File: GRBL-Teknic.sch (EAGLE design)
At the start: 65 parts, among them IC3 LM1117, J1 POWER_JACKOVERPASTE_REDBOARD_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, J2 ICSP, Q1 ZXMP6A13FTA, Q2 2N7002PW, U1 FT231XS, U2 MIC5205, U3 ATMEGA328, Y1 16MHz

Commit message: working from adafruit metro now, simpest i could find
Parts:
- removed AD: (no value), SparkFun:M06SMD-STRAIGHT-COMBO
- removed C1, C14, C8: 0.1uF, SparkFun:CAP0603-CAP
- removed C13: 47pF, SparkFun-Capacitors:47PF-50V-5%(0603)
- removed C7: 1uF, SparkFun:CAP0603-CAP
- removed D1: MBRA140, SparkFun:DIODE-SCHOTTKY_
- removed F1: 500mA, SparkFun:PTCSMD
- removed FRAME2: FRAME-LETTER, SparkFun-Aesthetics:FRAME-LETTER
- removed IC3: LM1117, Testing:V_REG_LM1117ALT1
- removed IOL: (no value), SparkFun:M08SMD-COMBO
- removed J1: POWER_JACKOVERPASTE_REDBOARD_0603, Testing:POWER_JACKOVERPASTE_REDBOARD_0603
- removed J2: ICSP, SparkFun-Connectors:AVR_SPI_PRG_6SMT_MALE
- removed JP1: LOGO-SFENW2, SparkFun-Aesthetics:LOGO-SFENW2
- removed JP10: (no value), SparkFun-Connectors:M08SMD-COMBO
- removed JP2: M10SMD_COMBO, SparkFun-Connectors:M10SMD_COMBO
- removed JP3, JP4, JP5, JP6: STAND-OFF, SparkFun:STAND-OFF
- removed JP7: LOGO-SFESK, SparkFun-Aesthetics:LOGO-SFESK
- removed JP8, JP9: FIDUCIAL1X2, SparkFun:FIDUCIAL1X2
- removed LED1: Blue, SparkFun-LED:LED1206-NS
- removed LED2: Green, SparkFun-LED:LED1206-NS
- removed LED3: Red, SparkFun-LED:LED1206-NS
- removed LED4: Yellow, SparkFun-LED:LED1206-NS
- removed Q1: ZXMP6A13FTA, SparkFun:MOSFET-PCHANNELSMD
- removed Q2: 2N7002PW, SparkFun-DiscreteSemi:MOSFET-NCHANNEL2N7002PW
- removed R1, R6, R7, R9: 1k, SparkFun:RESISTOR0603-RES
- removed R10: 27, SparkFun-Resistors:RESISTOR0603-RES
- removed R12, R3: 10k, SparkFun:RESISTOR0603-RES
- removed R14: 715, SparkFun:RESISTOR0603-RES
- removed R15: 240, SparkFun:RESISTOR0603-RES
- removed S1: RESET, SparkFun:TAC_SWITCHSMD
- removed TP1, TP2, TP3, TP4, TP5, TP6: TP-3x5, SparkFun-Passives:TEST-POINT3X5
- removed U$13: USB-MINIB-5PIN, SparkFun-Connectors:USB-MINIB-5PIN
- removed U$16: OSHW-LOGOS, SparkFun-Aesthetics:OSHW-LOGOS
- removed U3: ATMEGA328, SparkFun:ATMEGA168
- removed Y1: 16MHz, SparkFun-FreqCtrl:RESONATORSMD
- added ATX-POWER: 35318-0620, con-molex-2:555X-6H
- added D3: MBR120, microbuilder:DIODE-SCHOTTKYSOD-123
- added L: RED, microbuilder:LED0805_NOOUTLINE
- added ON: GREEN, microbuilder:LED0805_NOOUTLINE
- added POWER1: 20610, microbuilder:HEADER-1X870MIL
- added RESET: KMR2, microbuilder:SWITCH_TACT_SMT4.6X2.8
- added RXLED, TXLED: YELLOW, microbuilder:LED0805_NOOUTLINE
- added U4: FT231XQ-x, microbuilder:FT231X
- added VSELECT: (no value), microbuilder:SOLDERJUMPER_2WAY
- added X-MOTOR, Y-MOTOR-1, Y-MOTOR-2, Y-MOTOR-3: 35318-0820, con-molex-2:555X-8H
- added X3: 20329, microbuilder:USB_W_SHIELD_20329
- added Y2: CSTCE16M0V53-R0 16MHZ, SmartPrj:RESONATORMU
- C10, C4: device SparkFun:CAP0603-CAP -> microbuilder:CAP_CERAMIC0805-NOOUTLINE
- C12, C2: value 0.1uF -> 10uF; device SparkFun:CAP0603-CAP -> microbuilder:CAP_CERAMIC0805-NOOUTLINE
- C15: value 10uF -> 0.1uF; device SparkFun-Capacitors:CAP_POL1206 -> microbuilder:CAP_CERAMIC0805-NOOUTLINE
- C3: device SparkFun:CAP_POL1206 -> microbuilder:CAP_CERAMIC0805-NOOUTLINE
- C5: value 47uF -> 0.1uF; device SparkFun:CAP_POLD -> microbuilder:CAP_CERAMIC_0805MP
- C6: value 10uF -> 0.1uF; device SparkFun:CAP_POL1206 -> microbuilder:CAP_CERAMIC0805-NOOUTLINE
- C9: value 47pF -> 0.1uF; device SparkFun-Capacitors:47PF-50V-5%(0603) -> microbuilder:CAP_CERAMIC0805-NOOUTLINE
- R11: value 10k -> 1K; device SparkFun:RESISTOR0603-RES -> microbuilder:RESISTOR0805_NOOUTLINE
- R2: value 1k -> 1K; device SparkFun:RESISTOR0603-RES -> microbuilder:RESISTOR_4PACK
- R4: value 10k -> 22; device SparkFun:RESISTOR0603-RES -> microbuilder:RESISTOR0805_NOOUTLINE
- R5: value 27 -> 22; device SparkFun-Resistors:RESISTOR0603-RES -> microbuilder:RESISTOR_0805MP
- R8: value 1k -> 10K; device SparkFun:RESISTOR0603-RES -> microbuilder:RESISTOR0805_NOOUTLINE
- U1: value FT231XS -> MIC5225-5.0; device SparkFun-DigitalIC:FT231XS -> microbuilder:VREG_SOT23-5
- U2: value MIC5205 -> ATmega328P-MU; device SparkFun:V_REG_LDOSMD -> microbuilder:ATMEGA328P
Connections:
- removed net 5V: C2.2, C3.+, C4.1, IC3.OUT, IC3.OUT@1, J2.2, JP10.4, JP10.7, Q1.S, R12.2, R15.2, R2.2, R3.2, R4.2, R6.1, R7.1, TP1.1, U2.EN, U2.IN, U3.AVCC, U3.VCC@1, U3.VCC@2
- removed net INSERT: J1.GND, Q1.G, R4.1
- removed net N$12: Q2.S, R11.1, U1.!DTR
- removed net N$15: IC3.ADJ, R14.2, R15.1
- removed net N$2: LED2.A, R2.1
- removed net N$8: LED3.A, R6.2
- removed net PWRIN: D1.A, J1.PWR
- removed net RX-I: IOL.1, R8.1, U3.PD0(RXD)
- removed net RXLED: LED4.C, U1.CBUS1
- removed net TX-O: IOL.2, R9.1, U3.PD1(TXD)
- removed net TXLED: LED3.C, U1.CBUS2
- removed net USBVCC: C12.1, C15.+, F1.2, Q1.D, U1.VCC
- removed net VUSB: C10.1, F1.1, U$13.VBUS
- new net +5V: C15.1, C2.2, D3.C, ON.A, POWER1.4, RXLED.A, TXLED.A, U1.OUT, U4.VCC, VSELECT.3
- new net IO0: R11.1, U2.(RXD)PD0
- new net N$5: R2G$2.2, RXLED.C
- new net N$9: R4.2, U4.USB_DM
- new net VBUS: D3.A, POWER1.1, X3CONN.VBUS
- new net VCCIO: C10.2, C6.2, R8.2, U2.AVCC, U2.VCC, VSELECT.2
- new net XTAL1: U2.XTAL1, Y2.3
- new net XTAL2: U2.XTAL2, Y2.1
- net 3.3V: now also C3.2, C9.1, POWER1.3, U4.3V3OUT(50MA), U4.RESET#, U4.VCCIO, VSELECT.1; no longer C14.1, C6.+, C7.1, JP10.5, Q2.G, R11.2, U1.!RESET, U1.3V3OUT, U1.VCCIO, U2.OUT
- net AD0: now also U2.(ADC0)PC0; no longer AD.1, U3.PC0(ADC0)
- net AD1: now also U2.(ADC1)PC1; no longer AD.2, U3.PC1(ADC1)
- net AD2: now also U2.(ADC2)PC2; no longer AD.3, U3.PC2(ADC2)
- net AD3: now also U2.(ADC3)PC3; no longer AD.4, U3.PC3(ADC3)
- net AD4/SDA: now also U2.(ADC4)PC4; no longer AD.5, JP2.2, U3.PC4(ADC4/SDA)
- net AD5/SCL: now also U2.(ADC5)PC5; no longer AD.6, JP2.1, U3.PC5(ADC5/SCL)
- net AREF: now also C4.2, POWER1.8, U2.AREF; no longer C1.1, JP2.3, U3.AREF
- net D+: now also R5.1, X3CONN.D+; no longer C9.1, R10.1, U$13.D+
- net D-: now also R4.1, X3CONN.D-; no longer C13.1, R5.1, U$13.D-
- net DTR: now also C5.1, U4.DTR#; no longer C8.1, Q2.D, R12.1
- net GND: now also ATX-POWER-4.S, C10.1, C15.2, C3.1, C4.1, C6.1, POWER1.5, POWER1.6, R2G$3.1, R2G$4.1, RESET.P, RESET.P1, U1.GND, U2.AGND, U4.CBUS3/SLEEP, U4.GND, X-MOTOR-5.S, X-MOTOR-6.S, X-MOTOR-7.S, X-MOTOR-8.S, X3CONN.GND, X3SHIELD.1, Y-MOTOR-1-5.S, Y-MOTOR-1-6.S, Y-MOTOR-1-7.S, Y-MOTOR-1-8.S, Y-MOTOR-2-5.S, Y-MOTOR-2-6.S, Y-MOTOR-2-7.S, Y-MOTOR-2-8.S, Y-MOTOR-3-5.S, Y-MOTOR-3-6.S, Y-MOTOR-3-7.S, Y-MOTOR-3-8.S, Y2.2; no longer C1.2, C10.2, C13.2, C14.2, C15.-, C3.-, C4.2, C5.-, C6.-, C7.2, J1.GNDBREAK, J2.6, JP10.2, JP10.3, JP2.4, LED1.C, LED2.C, R14.1, S1.1, S1.2, TP3.1, U$13.GND, U$13.MTN1, U$13.MTN2, U$13.MTN3, U$13.MTN4, U1.GND@16, U1.GND@6, U3.AGND, U3.GND@1, U3.GND@2, Y1.2
- net IO2: now also U2.(INT0)PD2, X-MOTOR-2.S; no longer IOL.3, U3.PD2(INT0)
- net IO3: now also U2.(INT1)PD3, Y-MOTOR-1-2.S, Y-MOTOR-2-2.S; no longer IOL.4, U3.PD3(INT1)
- net IO4: now also U2.(TO)PD4, Y-MOTOR-3-2.S; no longer IOL.5, U3.PD4(XCK/T0)
- net IO5: now also U2.(T1)PD5, X-MOTOR-3.S; no longer IOL.6, U3.PD5(T1)
- net IO6: now also U2.(AIN0)PD6, Y-MOTOR-1-3.S, Y-MOTOR-2-3.S; no longer IOL.7, U3.PD6(AIN0)
- net IO7: now also U2.(AIN1)PD7, Y-MOTOR-3-3.S; no longer IOL.8, U3.PD7(AIN1)
- net IO8: now also U2.(ICP)PB0, X-MOTOR-4.S, Y-MOTOR-1-4.S, Y-MOTOR-2-4.S, Y-MOTOR-3-4.S; no longer JP2.10, U3.PB0(ICP)
- net IO9: now also U2.(OC1)PB1; no longer JP2.9, U3.PB1(OC1A)
- net MISO: now also U2.(MISO)PB4; no longer J2.1, JP2.6, TP4.1, U3.PB4(MISO)
- net MOSI: now also U2.(MOSI)PB3; no longer J2.4, JP2.7, TP2.1, U3.PB3(MOSI/OC2)
- net N$1: now also L.C, R2G$4.2; no longer LED1.A, R1.2
- net N$10: now also R5.2, U4.UDB_DP; no longer LED4.A, R7.2
- net N$3: now also ON.C, R2G$3.2; no longer U3.PB6(XTAL1/TOSC1), Y1.1
- net N$4: now also R2G$2.1, U4.CBUS1/RXLED; no longer U3.PB7(XTAL2/TOSC2), Y1.3
- net N$6: now also R2G$1.1, U4.CBUS2/TXLED; no longer R5.2, U1.USBDM
- net N$7: now also R2G$1.2, TXLED.C; no longer R10.2, U1.USBDP
- net RESET: now also C5.2, POWER1.2, R8.1, RESET.S, RESET.S1, U2.RESET; no longer C8.2, J2.5, JP10.6, R3.1, S1.3, S1.4, TP6.1, U3.PC6(/RESET)
- net RXD: now also R11.2, U4.TXD-OUT; no longer R9.2, U1.RXD
- net SCK: now also L.A, U2.(SCK)PB5; no longer J2.3, JP2.5, R1.1, TP5.1, U3.PB5(SCK)
- net SS: now also U2.(SS)PB2; no longer JP2.8, U3.PB2(SS/OC1B)
- net TXD: now also U2.(TXD)PD1, U4.RXD-IN; no longer R8.2, U1.TXD
- net VIN: now also ATX-POWER-1.S, C12.1, POWER1.7, U1.EN, U1.IN; no longer C5.+, D1.C, IC3.IN, JP10.1
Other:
- note added: "ATMEGA328 MCU"
- note added: "DTR triggers reset"
- note added: "Default = 5V Cut trace and solder to 3V3 to change"
- note added: "IO LEVEL SELECTION"
- note added: "POWER LED"
- note added: "POWER SUPPLY: 3.3V"
- note added: "POWER SUPPLY: 5V"
- note added: "SCK LED"
- note added: "Teknic Motor Connectors"
- note added: "USB/Serial Bridge"
- note removed: "3.3V 150mA Out"
- note removed: "ATmega328"
- note removed: "Based on Arduino by: M.Banzi, D.Cuartielles, T.Igoe, G.Martino, D.Mellis"
- note removed: "FT231XS (USB-to-Serial Converter)"
- note removed: "Jim Lindblom"
- note removed: "Power Supply"
- note removed: "v21"
- moved on the sheet: C10, C12, C2, C4, C9

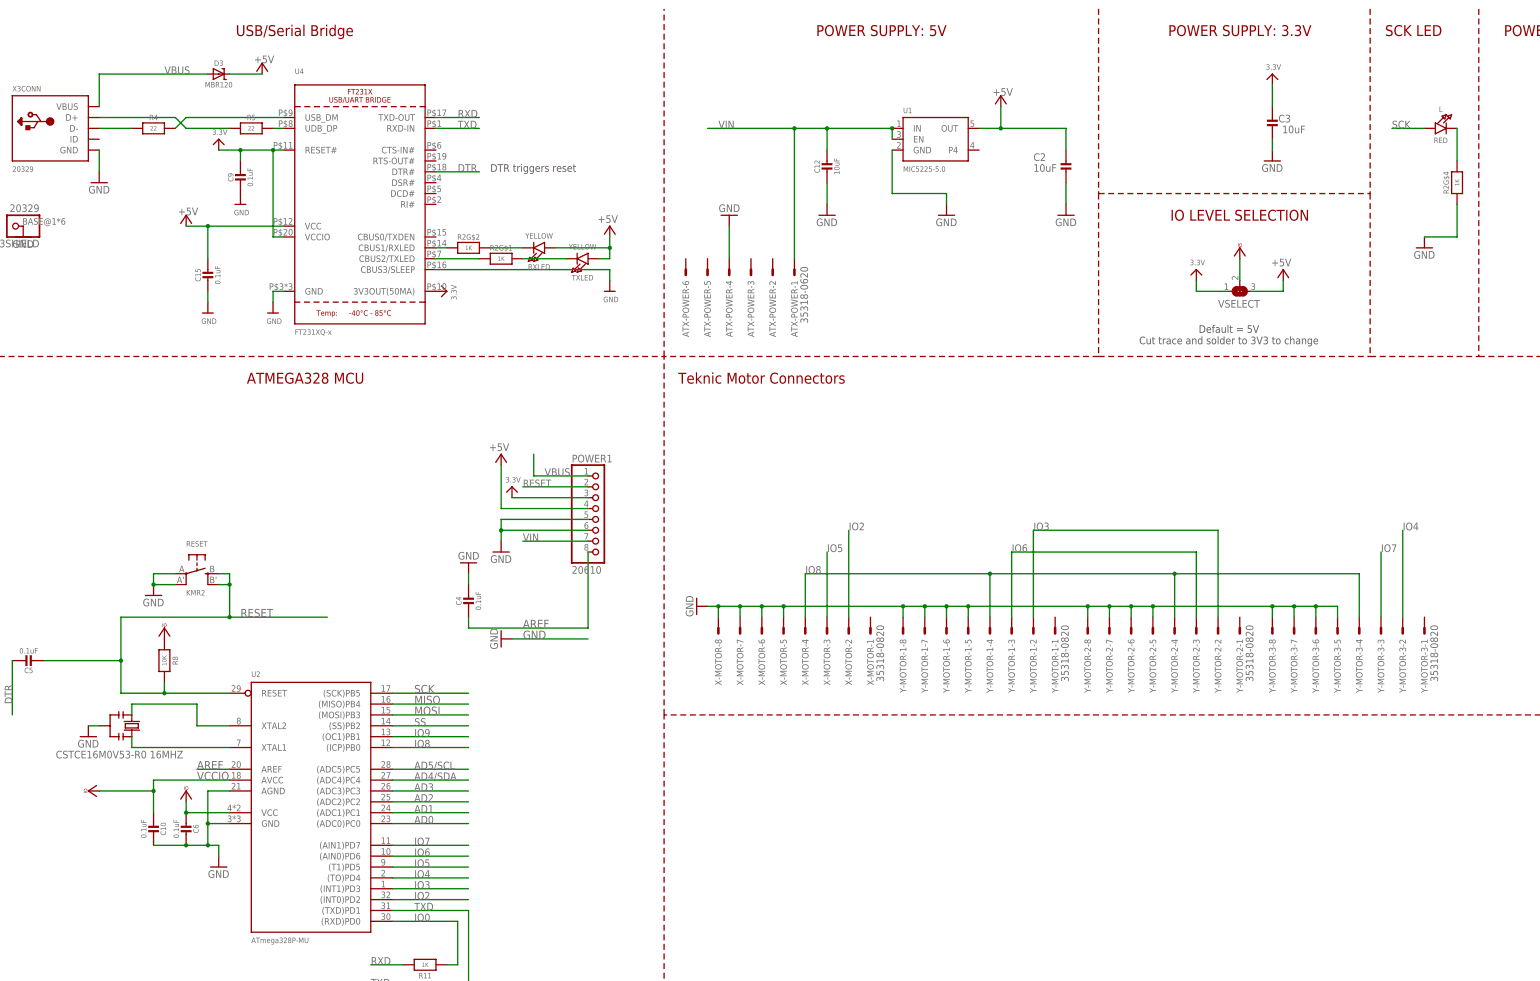
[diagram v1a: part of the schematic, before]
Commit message: added in motor and limit connectors
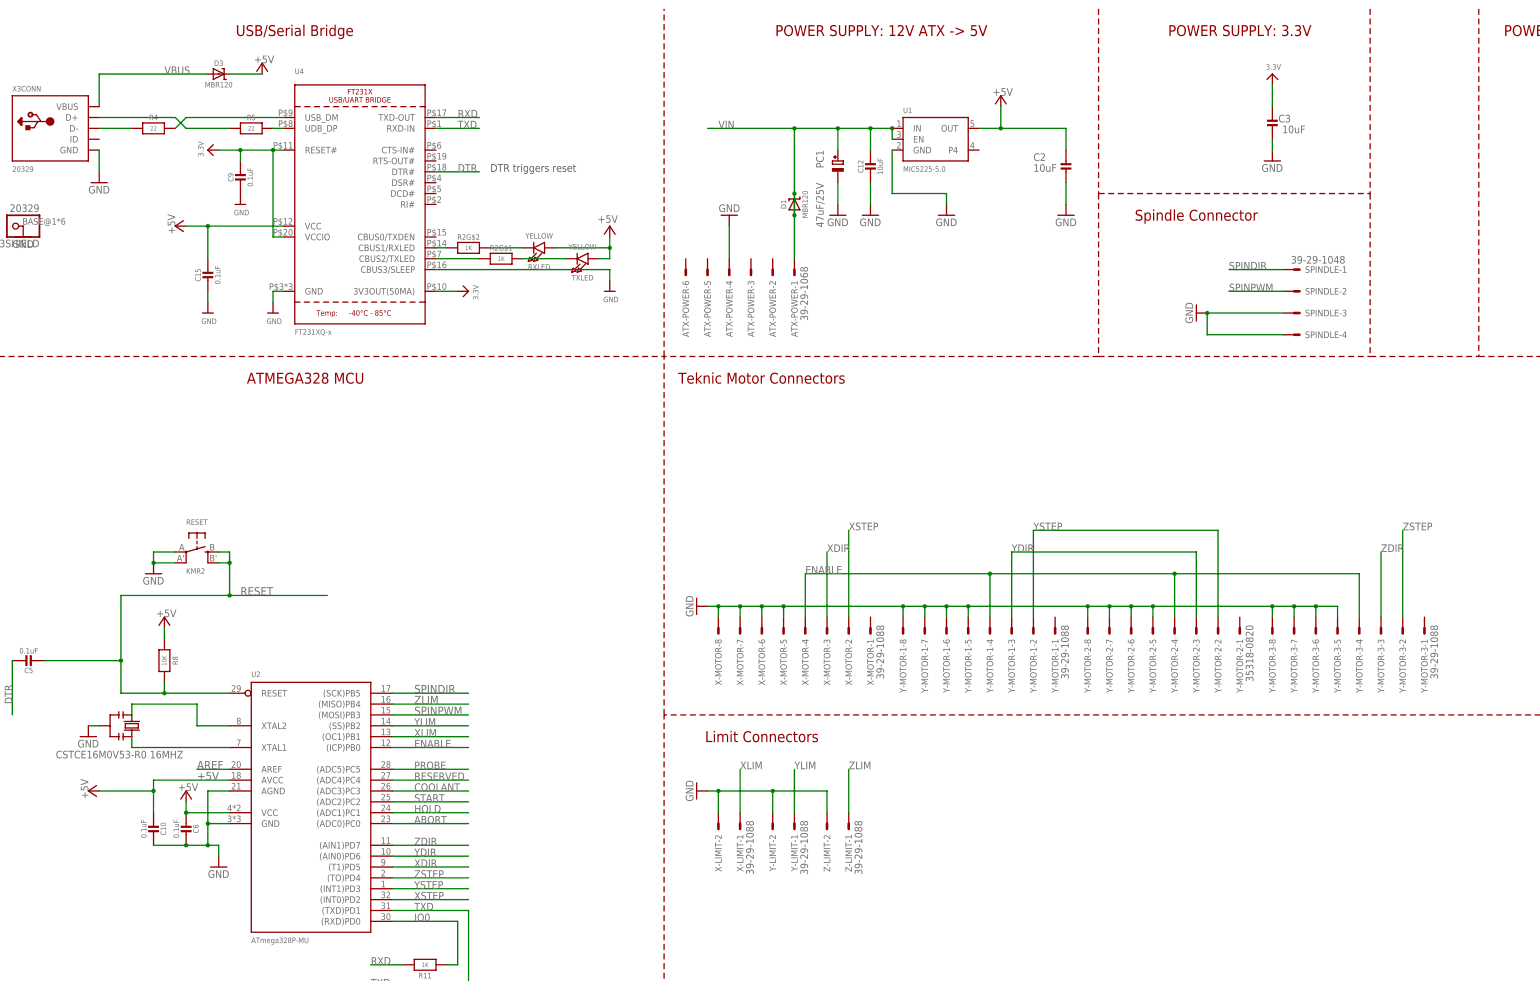
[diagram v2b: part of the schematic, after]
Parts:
- removed C4: 0.1uF, microbuilder:CAP_CERAMIC0805-NOOUTLINE
- removed L: RED, microbuilder:LED0805_NOOUTLINE
- removed POWER1: 20610, microbuilder:HEADER-1X870MIL
- removed VSELECT: (no value), microbuilder:SOLDERJUMPER_2WAY
- added D1: MBR120, microbuilder:DIODE-SCHOTTKYSOD-123
- added PC1: 47uF/25V, microbuilder:CAP_ELECTROLYTICPANASONIC_D
- added SPINDLE: 39-29-1048, con-molex-2:555X-4H
- added X-LIMIT, Y-LIMIT, Z-LIMIT: 39-29-1088, con-molex-2:555X-2H
- ATX-POWER: value 35318-0620 -> 39-29-1068
- X-MOTOR, Y-MOTOR-1, Y-MOTOR-3: value 35318-0820 -> 39-29-1088
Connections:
- net AD0 renamed ABORT
- net AD1 renamed HOLD
- net AD2 renamed START
- net AD3 renamed COOLANT
- net AD4/SDA renamed RESERVED
- net AD5/SCL renamed PROBE
- net IO2 renamed XSTEP
- net IO3 renamed YSTEP
- net IO4 renamed ZSTEP
- net IO5 renamed XDIR
- net IO6 renamed YDIR
- net IO7 renamed ZDIR
- net IO8 renamed ENABLE
- removed net IO9: U2.(OC1)PB1
- removed net MISO: U2.(MISO)PB4
- removed net MOSI: U2.(MOSI)PB3
- removed net N$1: L.C, R2G$4.2
- removed net SCK: L.A, U2.(SCK)PB5
- removed net SS: U2.(SS)PB2
- removed net VCCIO: C10.2, C6.2, R8.2, U2.AVCC, U2.VCC, VSELECT.2
- new net SPINDIR: SPINDLE-1.S, U2.(SCK)PB5
- new net SPINPWM: SPINDLE-2.S, U2.(MOSI)PB3
- new net XLIM: U2.(OC1)PB1, X-LIMIT-1.S
- new net YLIM: U2.(SS)PB2, Y-LIMIT-1.S
- new net ZLIM: U2.(MISO)PB4, Z-LIMIT-1.S
- net +5V: now also C10.2, C6.2, R8.2, U2.AVCC, U2.VCC; no longer POWER1.4, VSELECT.3
- net 3.3V: no longer POWER1.3, VSELECT.1
- net AREF: no longer C4.2, POWER1.8
- net GND: now also PC1.-, SPINDLE-3.S, SPINDLE-4.S, X-LIMIT-2.S, Y-LIMIT-2.S, Z-LIMIT-2.S; no longer C4.1, POWER1.5, POWER1.6, R2G$4.1
- net RESET: no longer POWER1.2
- net VBUS: no longer POWER1.1
- net VIN: now also D1.A, D1.C, PC1.+; no longer POWER1.7
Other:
- note added: "Limit Connectors"
- note added: "POWER SUPPLY: 12V ATX -> 5V"
- note added: "Spindle Connector"
- note removed: "Default = 5V Cut trace and solder to 3V3 to change"
- note removed: "IO LEVEL SELECTION"
- note removed: "POWER SUPPLY: 5V"
- note removed: "SCK LED"
- moved on the sheet: C12, RESET

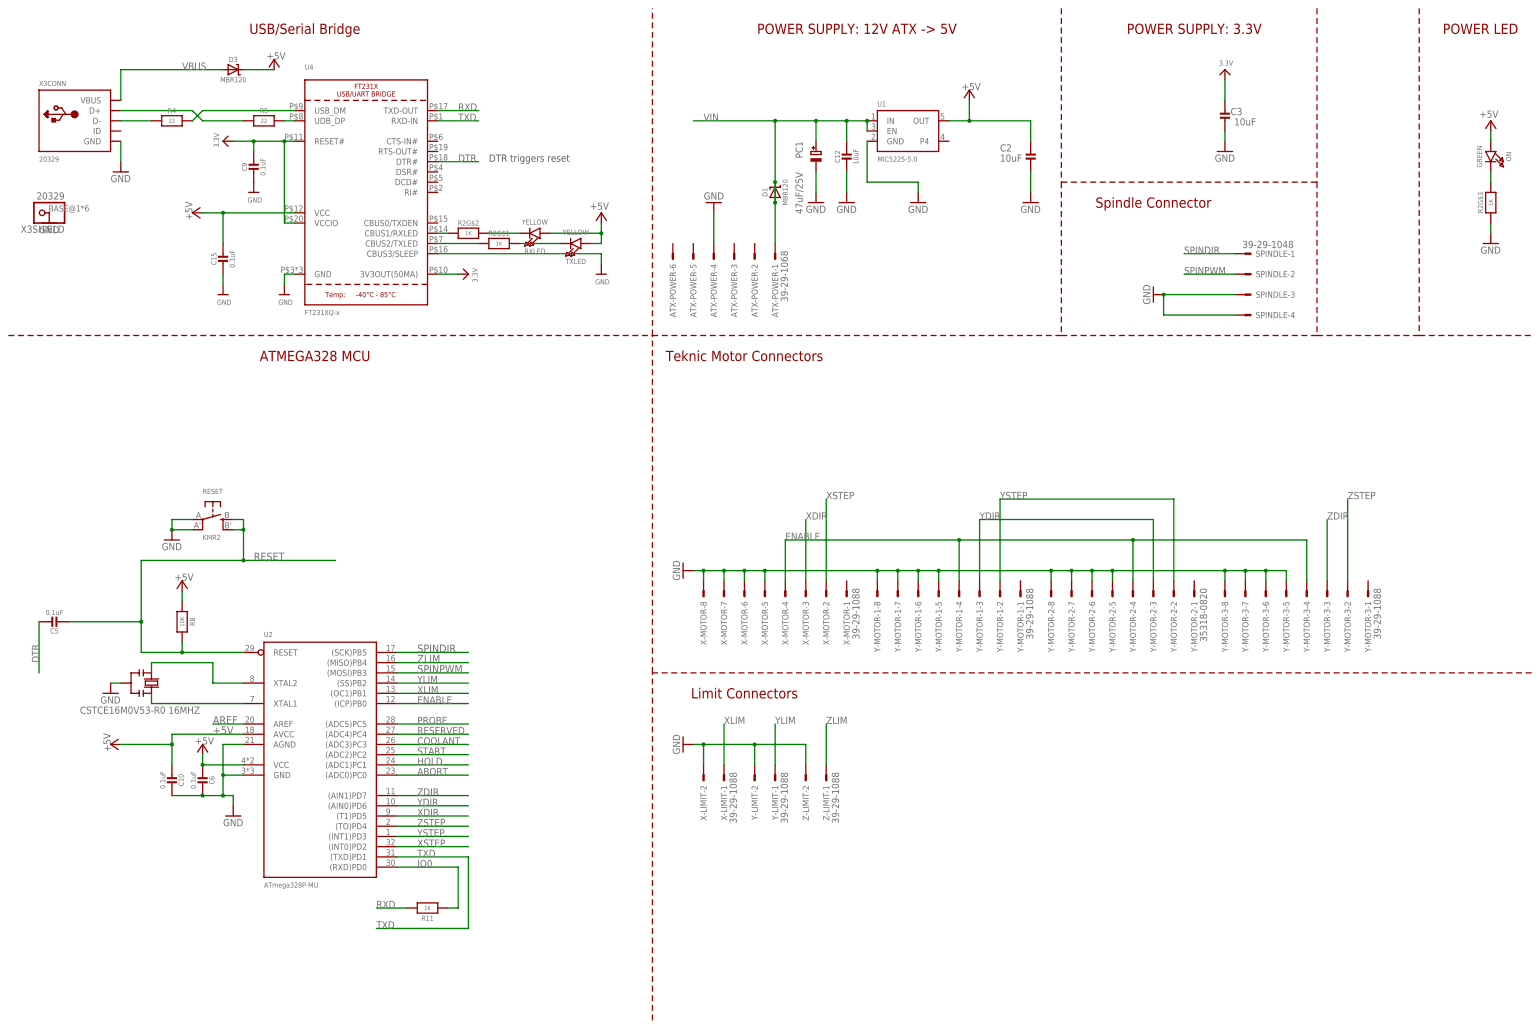
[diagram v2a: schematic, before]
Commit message: fixes #1 fixes #2
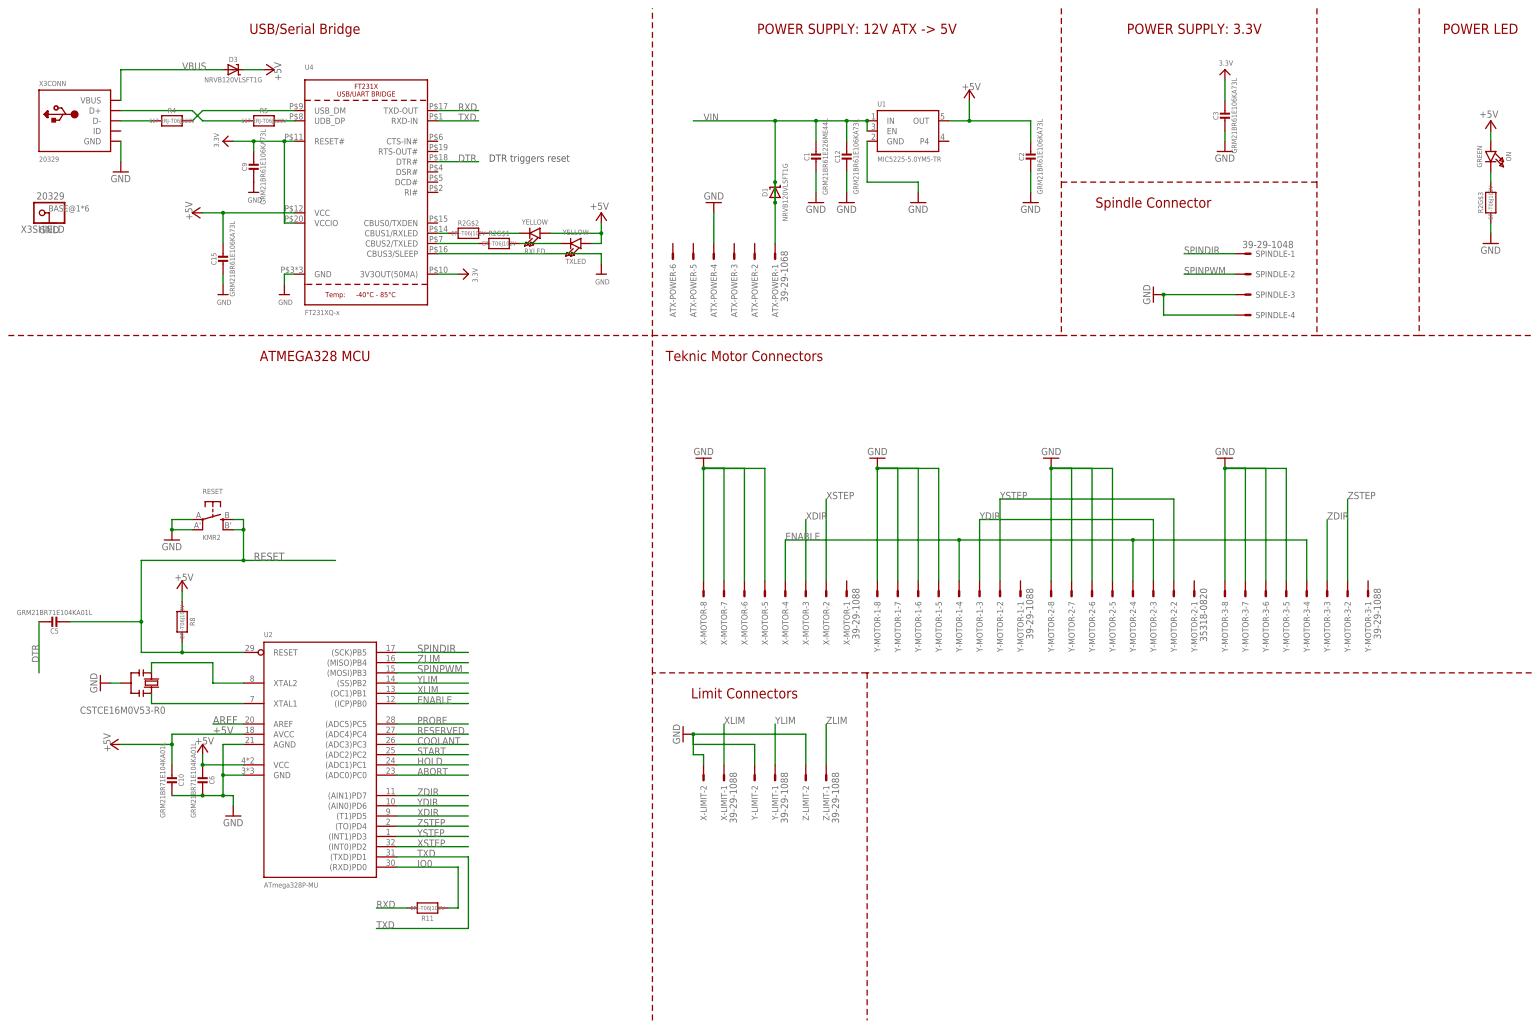
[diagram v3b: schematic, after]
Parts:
- removed PC1: 47uF/25V, microbuilder:CAP_ELECTROLYTICPANASONIC_D
- added C1: GRM21BR61E226ME44L, microbuilder:CAP_CERAMIC0805-NOOUTLINE
- C10, C5, C6: value 0.1uF -> GRM21BR71E104KA01L
- C12, C2, C3: value 10uF -> GRM21BR61E106KA73L
- C15, C9: value 0.1uF -> GRM21BR61E106KA73L
- D1, D3: value MBR120 -> NRVB120VLSFT1G
- R11, R2: value 1K -> ERJ-T06J102V
- R4, R5: value 22 -> 667-ERJ-T06J220V
- R8: value 10K -> ERJ-T06J103V
- U1: value MIC5225-5.0 -> MIC5225-5.0YM5-TR
- Y2: value CSTCE16M0V53-R0 16MHZ -> CSTCE16M0V53-R0
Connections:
- net +5V: now also C2.1; no longer C2.2
- net 3.3V: now also C3.1; no longer C3.2
- net GND: now also C1.2, C2.2, C3.2; no longer C2.1, C3.1, PC1.-
- net VIN: now also C1.1; no longer PC1.+
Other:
- moved on the sheet: C2, C3
